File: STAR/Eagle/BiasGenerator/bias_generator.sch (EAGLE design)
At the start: 24 parts, among them J1 J30J-9J30, T1 750311838, U1 LT8300, U2 LT8330

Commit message: half done bias board
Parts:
- removed C3: (no value), resistor:C-USC1210
- removed D1: MMSZ5266BT1G, AR_diode:ZENERSOD123
- removed D2: BAV20W, AR_diode:SCHOTTKYSOD323
- removed D3: SBR0560S1, AR_diode:SCHOTTKYSOD123
- removed R2: 407k, resistor:R-US_R0603
- removed R3: 1k, resistor:R-US_R0603
- removed T1: 750311838, AR_transformer:750311838
- removed U1: LT8300, AR_IC:LT8300
- added L2, L3: 82nH, resistor:L-US
- added U$1: DFT7160-105B, Filtering:DFT7160-105B
- C1: value 22uF -> .1uF; device AR_passives:CAPACITORC3025 -> resistor:C-USC0603
- C2: value 1uF -> .1uF; device AR_passives:CAPACITORC0603 -> resistor:C-USC0603
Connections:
- removed net +20V: C3.1, C5.1, D3.C, L1.1, U2.EN, U2.VCC
- removed net N$2: R2.1, U1.FB
- removed net N$3: R2.2, R3.1
- removed net N$4: D2.A, R3.2, T1.PB, U1.SW
- removed net N$5: D3.A, T1.S2B
- new net +50V_FILT: C2.1, L3.2
- new net VCC_FILT: C1.1, C5.1, L1.1, L2.2, U2.EN, U2.VCC
- net +50V: now also L3.1
- net GND: no longer C3.2, T1.S2A, U1.GND
- net N$1: now also L2.1, U$1.P$2, U$1.P$4; no longer D1.C, D2.C
- net VCC: now also U$1.P$1, U$1.P$3; no longer C1.1, C2.1, D1.A, T1.PA, U1.EN, U1.VCC
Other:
- note added: "Filter Network"
- note removed: "ISOLATION STAGE"
- moved on the sheet: C1, C2

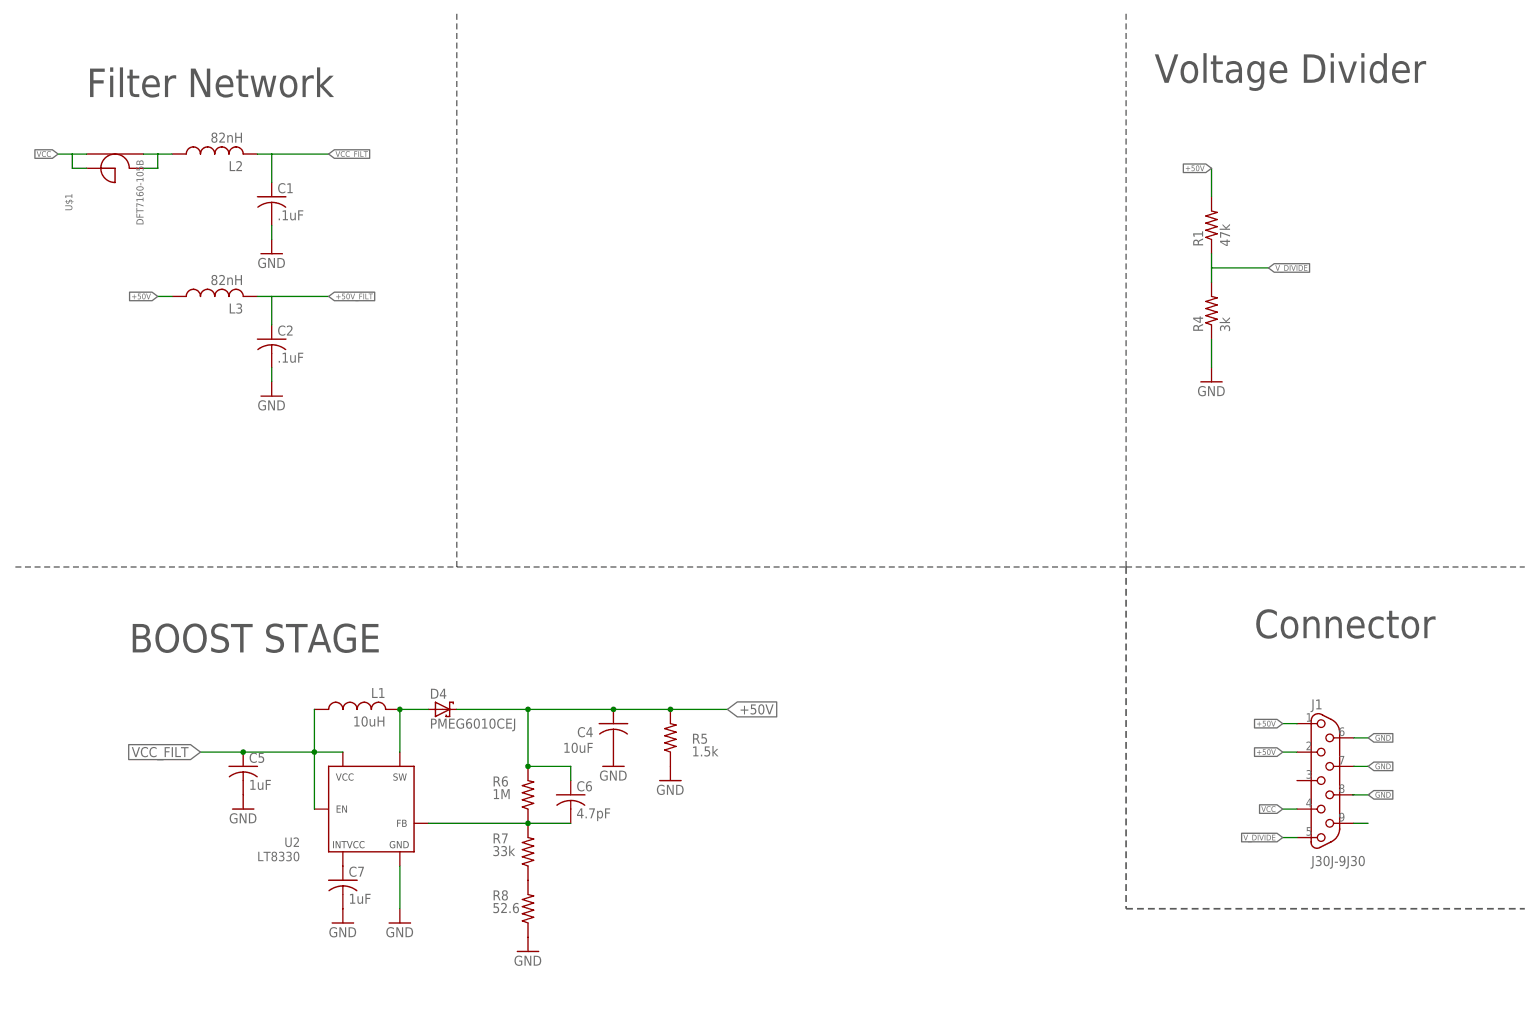
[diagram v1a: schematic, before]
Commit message: Added analog isolator to bias and revised connector
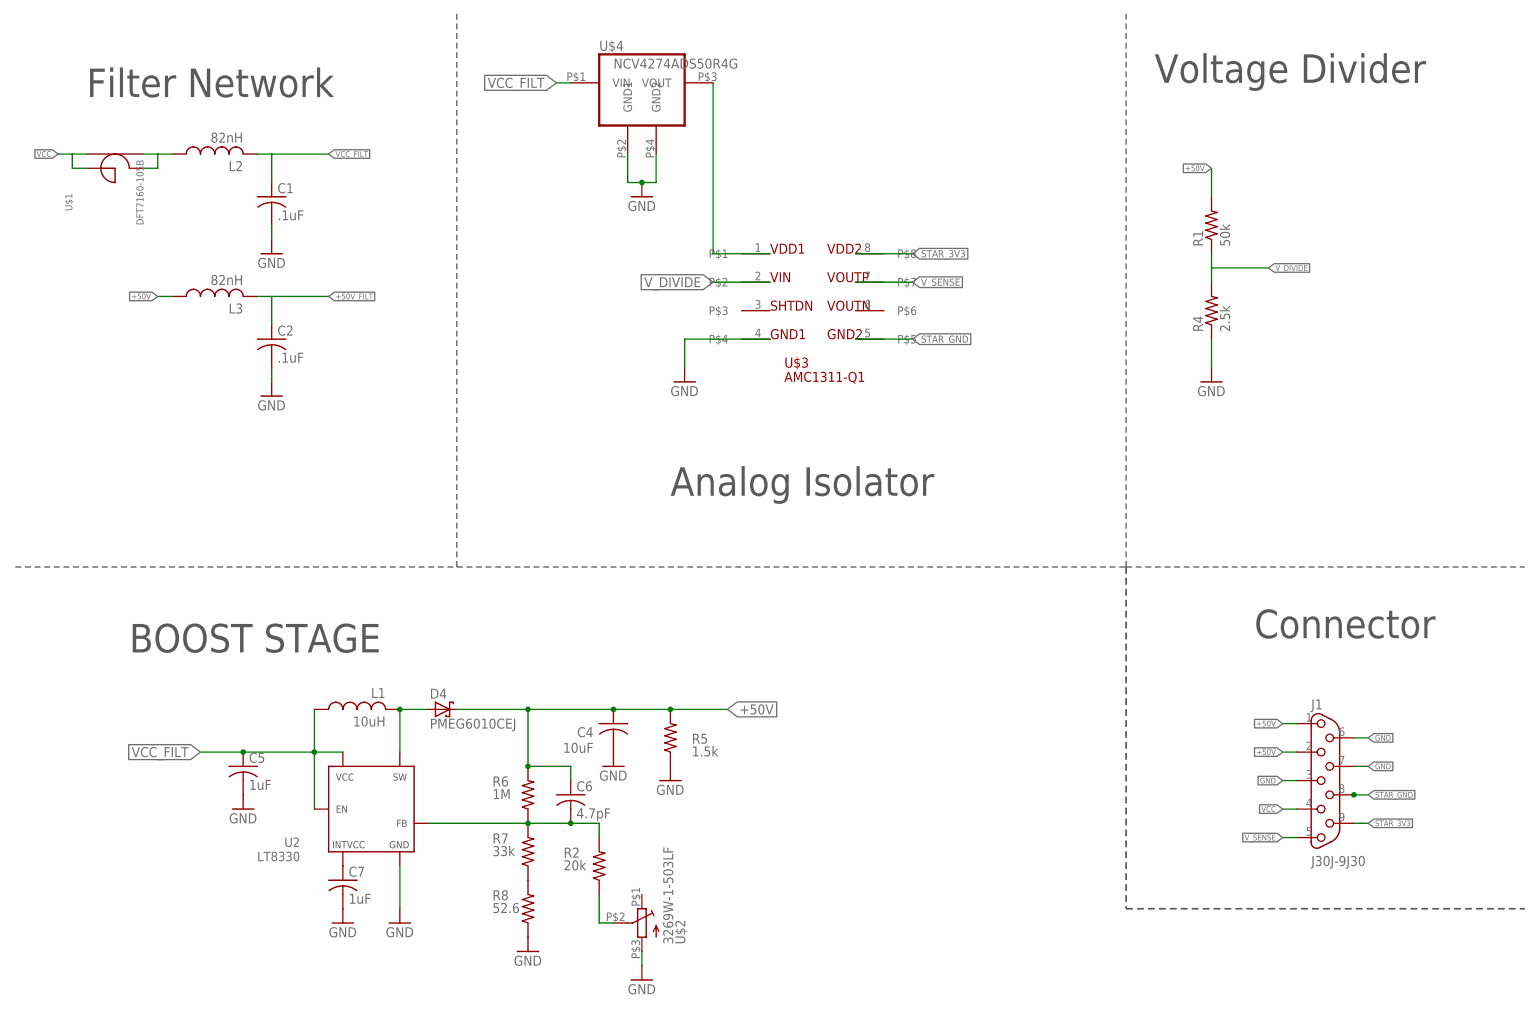
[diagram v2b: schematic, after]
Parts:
- added R2: 20k, resistor:R-US_R0603
- added U$2: 3269W-1-503LF, Filtering:3269W-1-503LF
- added U$3: AMC1311-Q1, Filtering:AMC1311-Q1
- added U$4: NCV4274ADS50R4G, Filtering:NCV4274ADS50R4G
- R1: value 47k -> 50k
- R4: value 3k -> 2.5k
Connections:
- removed net N$10: J1.9
- new net N$2: R2.1, U$2.P$2
- new net N$4: U$3.P$1, U$4.VOUT
- new net STAR_3V3: J1.9, U$3.P$8
- new net STAR_GND: J1.8, U$3.P$5
- new net V_SENSE: J1.5, U$3.P$7
- net GND: now also J1.3, U$2.P$3, U$3.P$4, U$4.GND1, U$4.GND2
- net N$9: now also R2.2
- net VCC_FILT: now also U$4.VIN
- net V_DIVIDE: now also U$3.P$2; no longer J1.5
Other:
- note added: "Analog Isolator"

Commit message: Finished routing new bias board rev 2.0. Fixed the choke configuration on that board.
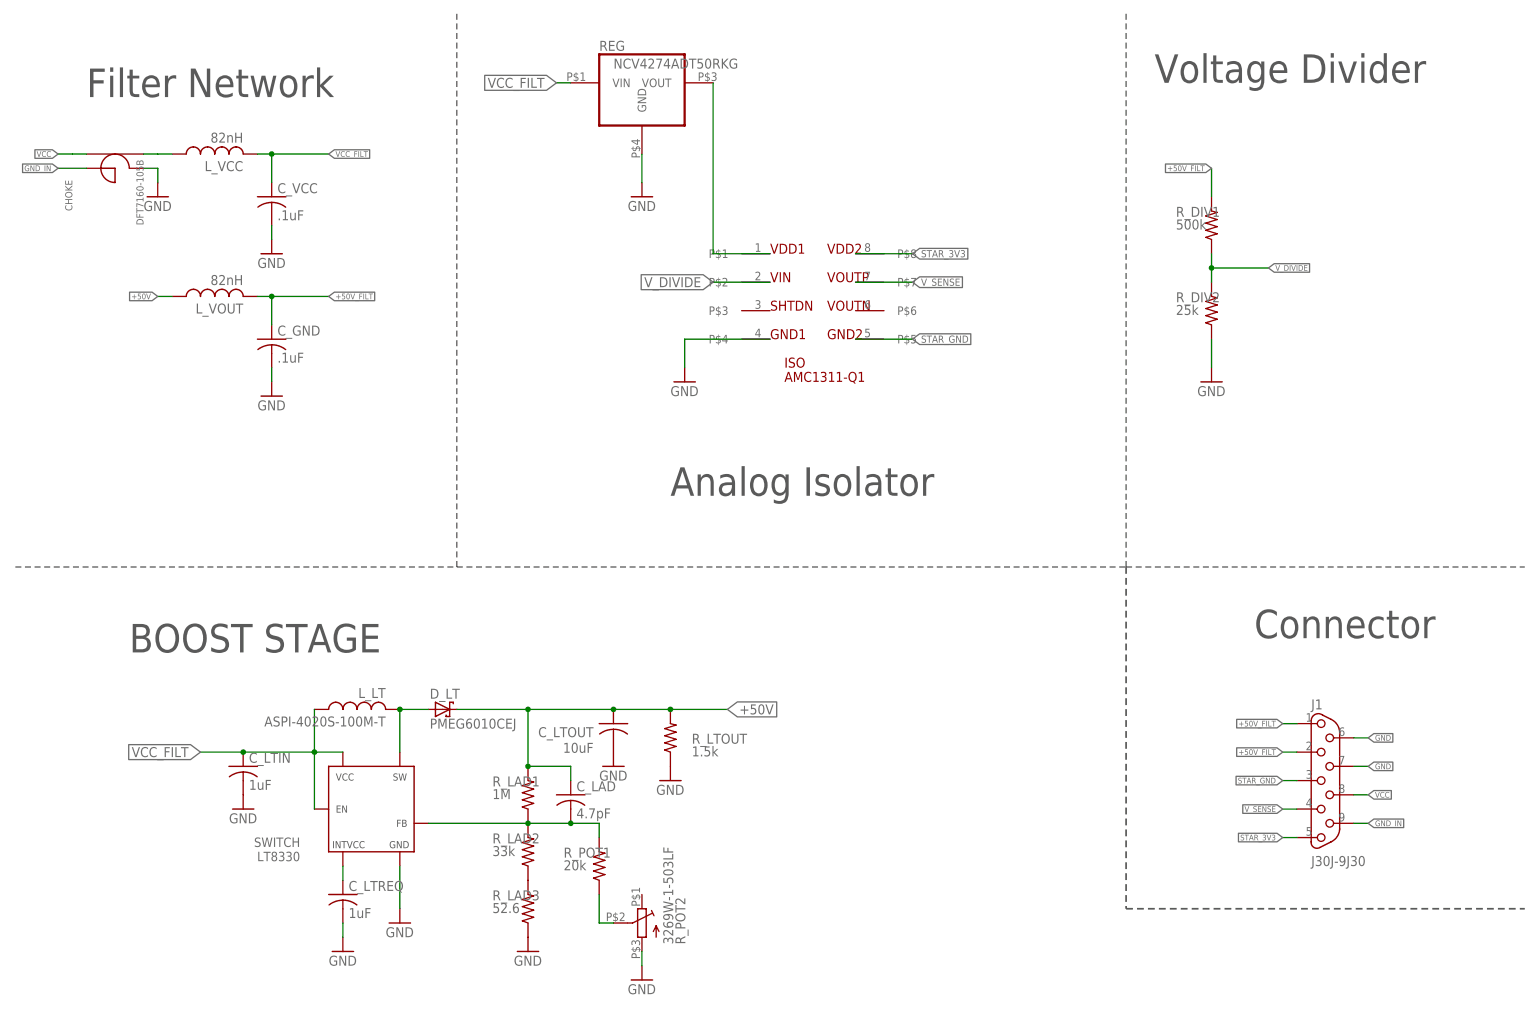
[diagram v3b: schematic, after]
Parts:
- removed C7: 1uF, AR_passives:CAPACITORC0603
- removed L1: 10uH, AR_passives:INDUCTORPQ2614
- removed R1: 50k, resistor:R-US_R2512
- removed R4: 2.5k, resistor:R-US_R2512
- removed U$4: NCV4274ADS50R4G, Filtering:NCV4274ADS50R4G
- added C_LTREQ: 1uF, AR_passives:CAPACITORC0603
- added L_LT: ASPI-4020S-100M-T, AR_passives:ASPI-4020S-100M-T
- added REG: NCV4274ADT50RKG, Filtering:NCV4274ADT50RKG
- added R_DIV1: 500k, resistor:R-US_R0603
- added R_DIV2: 25k, resistor:R-US_R0603
- renumbered C1 to C_VCC, C2 to C_GND, C4 to C_LTOUT, C5 to C_LTIN, C6 to C_LAD, D4 to D_LT, L2 to L_VCC, L3 to L_VOUT, R2 to R_POT1, R5 to R_LTOUT, R6 to R_LAD1, R7 to R_LAD2, R8 to R_LAD3, U$1 to CHOKE, U$2 to R_POT2, U$3 to ISO, U2 to SWITCH
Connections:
- net N$9 renamed FBX
- removed net N$4: ISO.P$1, U$4.VOUT
- removed net N$6: C7.1, SWITCH.INTVCC
- removed net N$7: D_LT.A, L1.2, SWITCH.SW
- new net 5V_REG: ISO.P$1, REG.VOUT
- new net GND_IN: CHOKE.P$1, J1.9
- new net INTVCC: C_LTREQ.1, SWITCH.INTVCC
- new net SW: D_LT.A, L_LT.2, SWITCH.SW
- net +50V: no longer J1.1, J1.2, R1.2
- net +50V_FILT: now also J1.1, J1.2, R_DIV1.2
- net GND: now also CHOKE.P$2, C_LTREQ.2, REG.GND, R_DIV2.1; no longer C7.2, J1.3, R4.1, U$4.GND1, U$4.GND2
- net N$1: no longer CHOKE.P$2
- net STAR_3V3: now also J1.5; no longer J1.9
- net STAR_GND: now also J1.3; no longer J1.8
- net VCC: now also J1.8; no longer CHOKE.P$1, J1.4
- net VCC_FILT: now also L_LT.1, REG.VIN; no longer L1.1, U$4.VIN
- net V_DIVIDE: now also R_DIV1.1, R_DIV2.2; no longer R1.1, R4.2
- net V_SENSE: now also J1.4; no longer J1.5

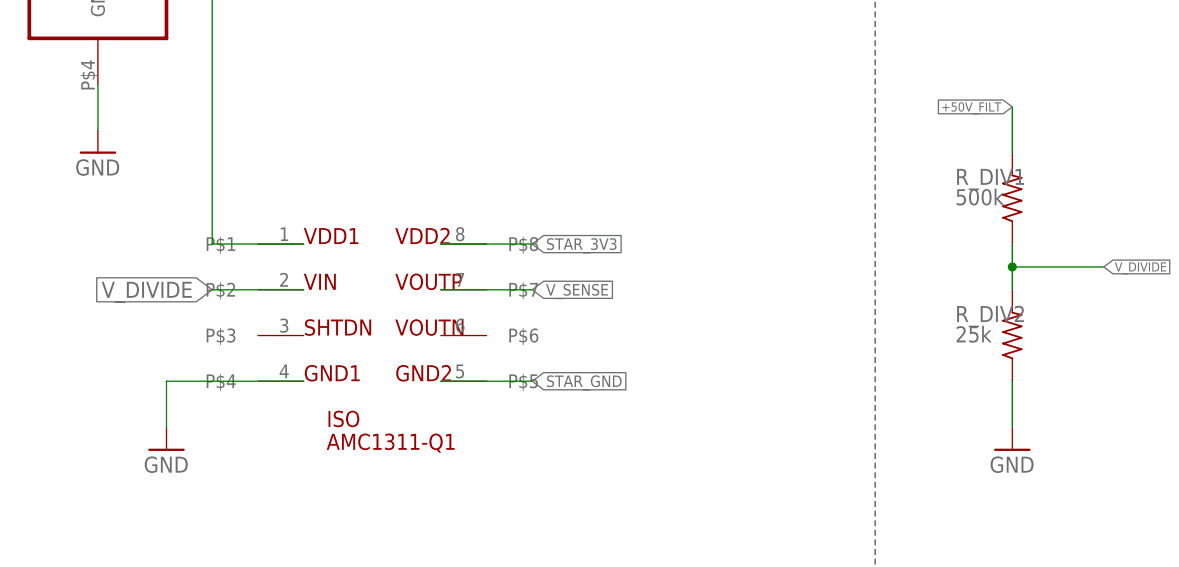
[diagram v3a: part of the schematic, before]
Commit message: Updated bias board and libraries to reflect the actual package used by the analog isolator
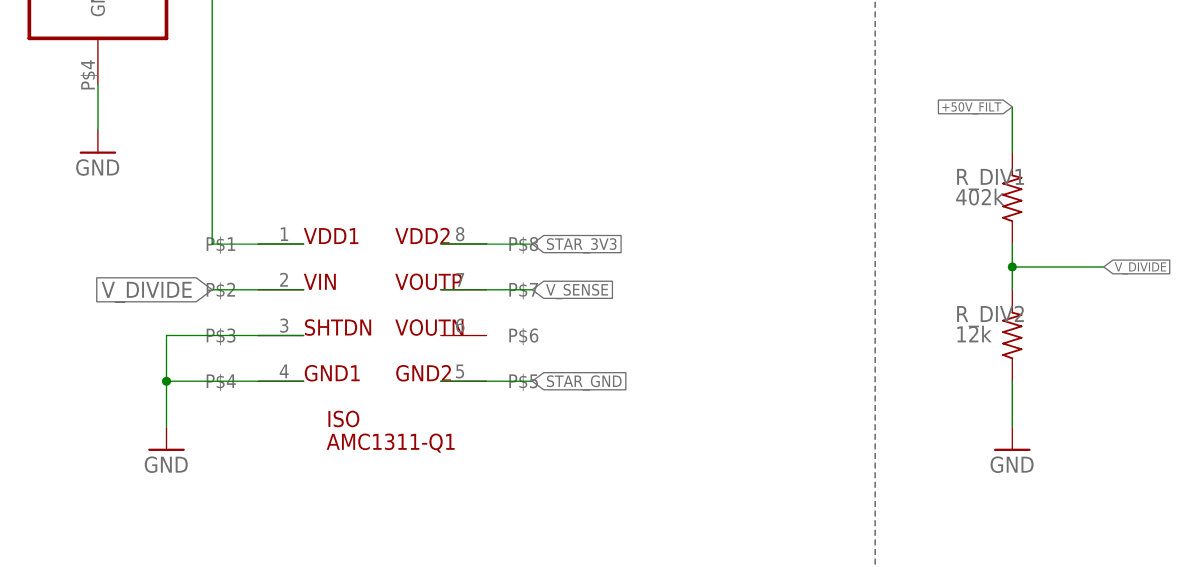
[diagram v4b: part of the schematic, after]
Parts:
- R_DIV1: value 500k -> 402k
- R_DIV2: value 25k -> 12k
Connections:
- net GND: now also CHOKE.L1OUT, ISO.P$3; no longer CHOKE.P$2
- net GND_IN: now also CHOKE.L1IN; no longer CHOKE.P$1
- net N$1: now also CHOKE.L2OUT; no longer CHOKE.P$4
- net VCC: now also CHOKE.L2IN; no longer CHOKE.P$3
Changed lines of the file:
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@@
 <part name="L_LT" library="AR_passives" deviceset="ASPI-4020S-100M-T" device=""/>
 <part name="REG" library="Filtering" deviceset="NCV4274ADT50RKG" device=""/>
-<part name="R_DIV1" library="resistor" deviceset="R-US_" device="R0603" value="500k"/>
-<part name="R_DIV2" library="resistor" deviceset="R-US_" device="R0603" value="25k"/>
+<part name="R_DIV1" library="resistor" deviceset="R-US_" device="R0603" value="402k"/>
+<part name="R_DIV2" library="resistor" deviceset="R-US_" device="R0603" value="12k"/>
 <part name="GND13" library="supply1" library_urn="urn:adsk.eagle:library:371" deviceset="GND" device=""/>
 </parts>
@@
 <net name="VCC" class="0">
 <segment>
-<pinref part="CHOKE" gate="G$1" pin="P$3"/>
+<pinref part="CHOKE" gate="G$1" pin="L2IN"/>
 <wire x1="17.78" y1="185.42" x2="15.24" y2="185.42" width="0.1524" layer="91"/>
 <wire x1="15.24" y1="185.42" x2="12.7" y2="185.42" width="0.1524" layer="91"/>
@@
 <wire x1="124.46" y1="152.4" x2="124.46" y2="147.32" width="0.1524" layer="91"/>
 <pinref part="GND5" gate="1" pin="GND"/>
+<pinref part="ISO" gate="G$1" pin="P$3"/>
+<wire x1="139.7" y1="157.48" x2="129.54" y2="157.48" width="0.1524" layer="91"/>
+<wire x1="129.54" y1="157.48" x2="124.46" y2="157.48" width="0.1524" layer="91"/>
+<wire x1="124.46" y1="157.48" x2="124.46" y2="152.4" width="0.1524" layer="91"/>
+<junction x="124.46" y="152.4"/>
 </segment>
 <segment>
@@
 </segment>
 <segment>
-<pinref part="CHOKE" gate="G$1" pin="P$2"/>
+<pinref part="CHOKE" gate="G$1" pin="L1OUT"/>
 <wire x1="27.94" y1="182.88" x2="30.48" y2="182.88" width="0.1524" layer="91"/>
 <wire x1="30.48" y1="182.88" x2="30.48" y2="180.34" width="0.1524" layer="91"/>
@@
 <segment>
 <pinref part="L_VCC" gate="G$1" pin="1"/>
-<pinref part="CHOKE" gate="G$1" pin="P$4"/>
+<pinref part="CHOKE" gate="G$1" pin="L2OUT"/>
 <wire x1="33.02" y1="185.42" x2="30.48" y2="185.42" width="0.1524" layer="91"/>
 <wire x1="30.48" y1="185.42" x2="27.94" y2="185.42" width="0.1524" layer="91"/>
@@
 <net name="GND_IN" class="0">
 <segment>
-<pinref part="CHOKE" gate="G$1" pin="P$1"/>
+<pinref part="CHOKE" gate="G$1" pin="L1IN"/>
 <wire x1="17.78" y1="182.88" x2="12.7" y2="182.88" width="0.1524" layer="91"/>
 <label x="12.7" y="182.88" size="1.016" layer="95" rot="MR0" xref="yes"/>
